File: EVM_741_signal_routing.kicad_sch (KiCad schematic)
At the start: 51 parts, among them J1 offset+, J10 out_a, J11 out_j, J12 out_j, J13 Vcc+_a, J14 Vcc-_a, J2 in-, J3 in+, J4 Vcc-, J5 offset-, J6 out, J7 Vcc+, J8 in+_a, J9 in-_a, Q1 MMBT3904, Q10 MMBT3904, Q11 MMBT3904, Q12 MMBT3906, Q13 MMBT3906, Q14 MMBT3904, Q15 MMBT3904, Q16 MMBT3904, Q17 MMBT3904, Q18 MMBT3904, Q2 MMBT3904, Q20 MMBT3906, Q22 MMBT3904, Q3 MMBT3906, Q4 MMBT3906, Q5 MMBT3904, Q6 MMBT3904, Q7 MMBT3904, Q8 MMBT3906, Q9 MMBT3906

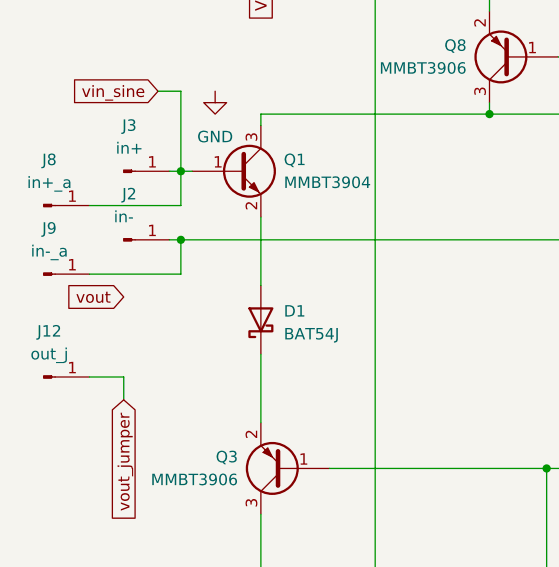
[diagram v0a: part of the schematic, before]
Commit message: added spice sim lib
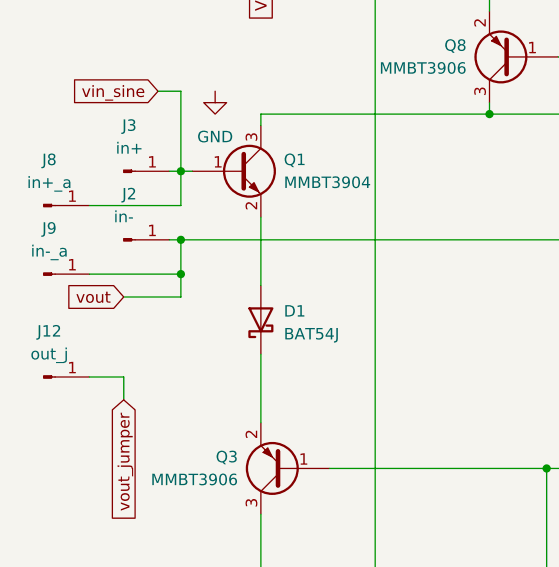
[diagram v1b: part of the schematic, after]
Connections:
- net vout: now also J2.1 (Pin_1), J9.1 (Pin_1), Q2.1 (B)
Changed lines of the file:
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@@
   (junction (at 182.88 58.42) (diameter 0) (color 0 0 0 0)
   )
+  (junction (at 34.29 57.15) (diameter 0) (color 0 0 0 0)
+  )
   (junction (at 55.88 21.59) (diameter 0) (color 0 0 0 0)
   )
@@
     (stroke (width 0) (type default))
   )
+  (wire (pts (xy 27.94 59.69) (xy 34.29 59.69))
+    (stroke (width 0) (type default))
+  )
   (wire (pts (xy 127 109.22) (xy 132.08 109.22))
     (stroke (width 0) (type default))
@@
   )
   (wire (pts (xy 233.68 63.5) (xy 233.68 78.74))
+    (stroke (width 0) (type default))
+  )
+  (wire (pts (xy 34.29 59.69) (xy 34.29 57.15))
     (stroke (width 0) (type default))
   )
@@
       (effects (font (size 1.27 1.27)) hide)
     )
-    (property "Sim.Library" "D:\\hw_things\\EVM_741_spice.lib" (at 43.18 62.23 0)
+    (property "Sim.Library" "${KIPRJMOD}\\EVM_741_spice.lib" (at 43.18 62.23 0)
       (effects (font (size 1.27 1.27)) hide)
     )
@@
       (effects (font (size 1.27 1.27)) (justify left) hide)
     )
-    (property "Sim.Library" "D:\\hw_things\\EVM_741_spice.lib" (at 205.74 58.42 0)
+    (property "Sim.Library" "${KIPRJMOD}\\EVM_741_spice.lib" (at 205.74 58.42 0)
       (effects (font (size 1.27 1.27)) hide)
     )
@@
       (effects (font (size 1.27 1.27)) (justify left) hide)
     )
-    (property "Sim.Library" "D:\\hw_things\\EVM_741_spice.lib" (at 180.34 91.44 0)
+    (property "Sim.Library" "${KIPRJMOD}\\EVM_741_spice.lib" (at 180.34 91.44 0)
       (effects (font (size 1.27 1.27)) hide)
     )
@@
       (effects (font (size 1.27 1.27)) hide)
     )
-    (property "Sim.Library" "D:\\hw_things\\EVM_741_spice.lib" (at 93.98 62.23 0)
+    (property "Sim.Library" "${KIPRJMOD}\\EVM_741_spice.lib" (at 93.98 62.23 0)
       (effects (font (size 1.27 1.27)) hide)
     )
@@
       (effects (font (size 1.27 1.27)) (justify left) hide)
     )
-    (property "Sim.Library" "D:\\hw_things\\EVM_741_spice.lib" (at 205.74 99.06 0)
+    (property "Sim.Library" "${KIPRJMOD}\\EVM_741_spice.lib" (at 205.74 99.06 0)
       (effects (font (size 1.27 1.27)) hide)
     )
@@
       (effects (font (size 1.27 1.27)) (justify left) hide)
     )
-    (property "Sim.Library" "D:\\hw_things\\EVM_741_spice.lib" (at 251.46 104.14 0)
+    (property "Sim.Library" "${KIPRJMOD}\\EVM_741_spice.lib" (at 251.46 104.14 0)
       (effects (font (size 1.27 1.27)) hide)
     )
@@
       (effects (font (size 1.27 1.27)) (justify left) hide)
     )
-    (property "Sim.Library" "D:\\hw_things\\EVM_741_spice.lib" (at 40.64 45.72 0)
+    (property "Sim.Library" "${KIPRJMOD}\\EVM_741_spice.lib" (at 40.64 45.72 0)
       (effects (font (size 1.27 1.27)) hide)
     )
@@
       (effects (font (size 1.27 1.27)) (justify left) hide)
     )
-    (property "Sim.Library" "D:\\hw_things\\EVM_741_spice.lib" (at 116.84 33.02 0)
+    (property "Sim.Library" "${KIPRJMOD}\\EVM_741_spice.lib" (at 116.84 33.02 0)
       (effects (font (size 1.27 1.27)) hide)
     )
@@
       (effects (font (size 1.27 1.27)) (justify left) hide)
     )
-    (property "Sim.Library" "D:\\hw_things\\EVM_741_spice.lib" (at 45.72 109.22 0)
+    (property "Sim.Library" "${KIPRJMOD}\\EVM_741_spice.lib" (at 45.72 109.22 0)
       (effects (font (size 1.27 1.27)) hide)
     )
@@
       (effects (font (size 1.27 1.27)) (justify left) hide)
     )
-    (property "Sim.Library" "D:\\hw_things\\EVM_741_spice.lib" (at 91.44 109.22 0)
+    (property "Sim.Library" "${KIPRJMOD}\\EVM_741_spice.lib" (at 91.44 109.22 0)
       (effects (font (size 1.27 1.27)) hide)
     )
@@
       (effects (font (size 1.27 1.27)) (justify left) hide)
     )
-    (property "Sim.Library" "D:\\hw_things\\EVM_741_spice.lib" (at 71.12 33.02 0)
+    (property "Sim.Library" "${KIPRJMOD}\\EVM_741_spice.lib" (at 71.12 33.02 0)
       (effects (font (size 1.27 1.27)) hide)
     )
@@
       (effects (font (size 1.27 1.27)) (justify left) hide)
     )
-    (property "Sim.Library" "D:\\hw_things\\EVM_741_spice.lib" (at 236.22 58.42 0)
+    (property "Sim.Library" "${KIPRJMOD}\\EVM_741_spice.lib" (at 236.22 58.42 0)
       (effects (font (size 1.27 1.27)) hide)
     )
@@
       (effects (font (size 1.27 1.27)) (justify left) hide)
     )
-    (property "Sim.Library" "D:\\hw_things\\EVM_741_spice.lib" (at 53.34 96.52 0)
+    (property "Sim.Library" "${KIPRJMOD}\\EVM_741_spice.lib" (at 53.34 96.52 0)
       (effects (font (size 1.27 1.27)) hide)
     )
@@
       (effects (font (size 1.27 1.27)) (justify left) hide)
     )
-    (property "Sim.Library" "D:\\hw_things\\EVM_741_spice.lib" (at 121.92 109.22 0)
+    (property "Sim.Library" "${KIPRJMOD}\\EVM_741_spice.lib" (at 121.92 109.22 0)
       (effects (font (size 1.27 1.27)) hide)
     )
@@
       (effects (font (size 1.27 1.27)) (justify left) hide)
     )
-    (property "Sim.Library" "D:\\hw_things\\EVM_741_spice.lib" (at 205.74 33.02 0)
+    (property "Sim.Library" "${KIPRJMOD}\\EVM_741_spice.lib" (at 205.74 33.02 0)
       (effects (font (size 1.27 1.27)) hide)
     )
@@
       (effects (font (size 1.27 1.27)) (justify left) hide)
     )
-    (property "Sim.Library" "D:\\hw_things\\EVM_741_spice.lib" (at 251.46 40.64 0)
+    (property "Sim.Library" "${KIPRJMOD}\\EVM_741_spice.lib" (at 251.46 40.64 0)
       (effects (font (size 1.27 1.27)) hide)
     )
@@
       (effects (font (size 1.27 1.27)) (justify left) hide)
     )
-    (property "Sim.Library" "D:\\hw_things\\EVM_741_spice.lib" (at 91.44 78.74 0)
+    (property "Sim.Library" "${KIPRJMOD}\\EVM_741_spice.lib" (at 91.44 78.74 0)
       (effects (font (size 1.27 1.27)) hide)
     )
@@
       (effects (font (size 1.27 1.27)) (justify left) hide)
     )
-    (property "Sim.Library" "D:\\hw_things\\EVM_741_spice.lib" (at 142.24 109.22 0)
+    (property "Sim.Library" "${KIPRJMOD}\\EVM_741_spice.lib" (at 142.24 109.22 0)
       (effects (font (size 1.27 1.27)) hide)
     )
@@
       (effects (font (size 1.27 1.27)) (justify left) hide)
     )
-    (property "Sim.Library" "D:\\hw_things\\EVM_741_spice.lib" (at 147.32 33.02 0)
+    (property "Sim.Library" "${KIPRJMOD}\\EVM_741_spice.lib" (at 147.32 33.02 0)
       (effects (font (size 1.27 1.27)) hide)
     )
@@
       (effects (font (size 1.27 1.27)) (justify left) hide)
     )
-    (property "Sim.Library" "D:\\hw_things\\EVM_741_spice.lib" (at 45.72 78.74 0)
+    (property "Sim.Library" "${KIPRJMOD}\\EVM_741_spice.lib" (at 45.72 78.74 0)
       (effects (font (size 1.27 1.27)) hide)
     )
@@
       (effects (font (size 1.27 1.27)) (justify left) hide)
     )
-    (property "Sim.Library" "D:\\hw_things\\EVM_741_spice.lib" (at 172.72 116.84 0)
+    (property "Sim.Library" "${KIPRJMOD}\\EVM_741_spice.lib" (at 172.72 116.84 0)
       (effects (font (size 1.27 1.27)) hide)
     )
@@
       (effects (font (size 1.27 1.27)) (justify left) hide)
     )
-    (property "Sim.Library" "D:\\hw_things\\EVM_741_spice.lib" (at 96.52 45.72 0)
-      (effects (font (size 1.27 1.27)) hide)
-    )
+    (property "Sim.Library" "${KIPRJMOD}\\EVM_741_spice.lib" (at 96.52 45.72 0)
+      (effects (font (size 1.27 1.27)) hide)
+    )

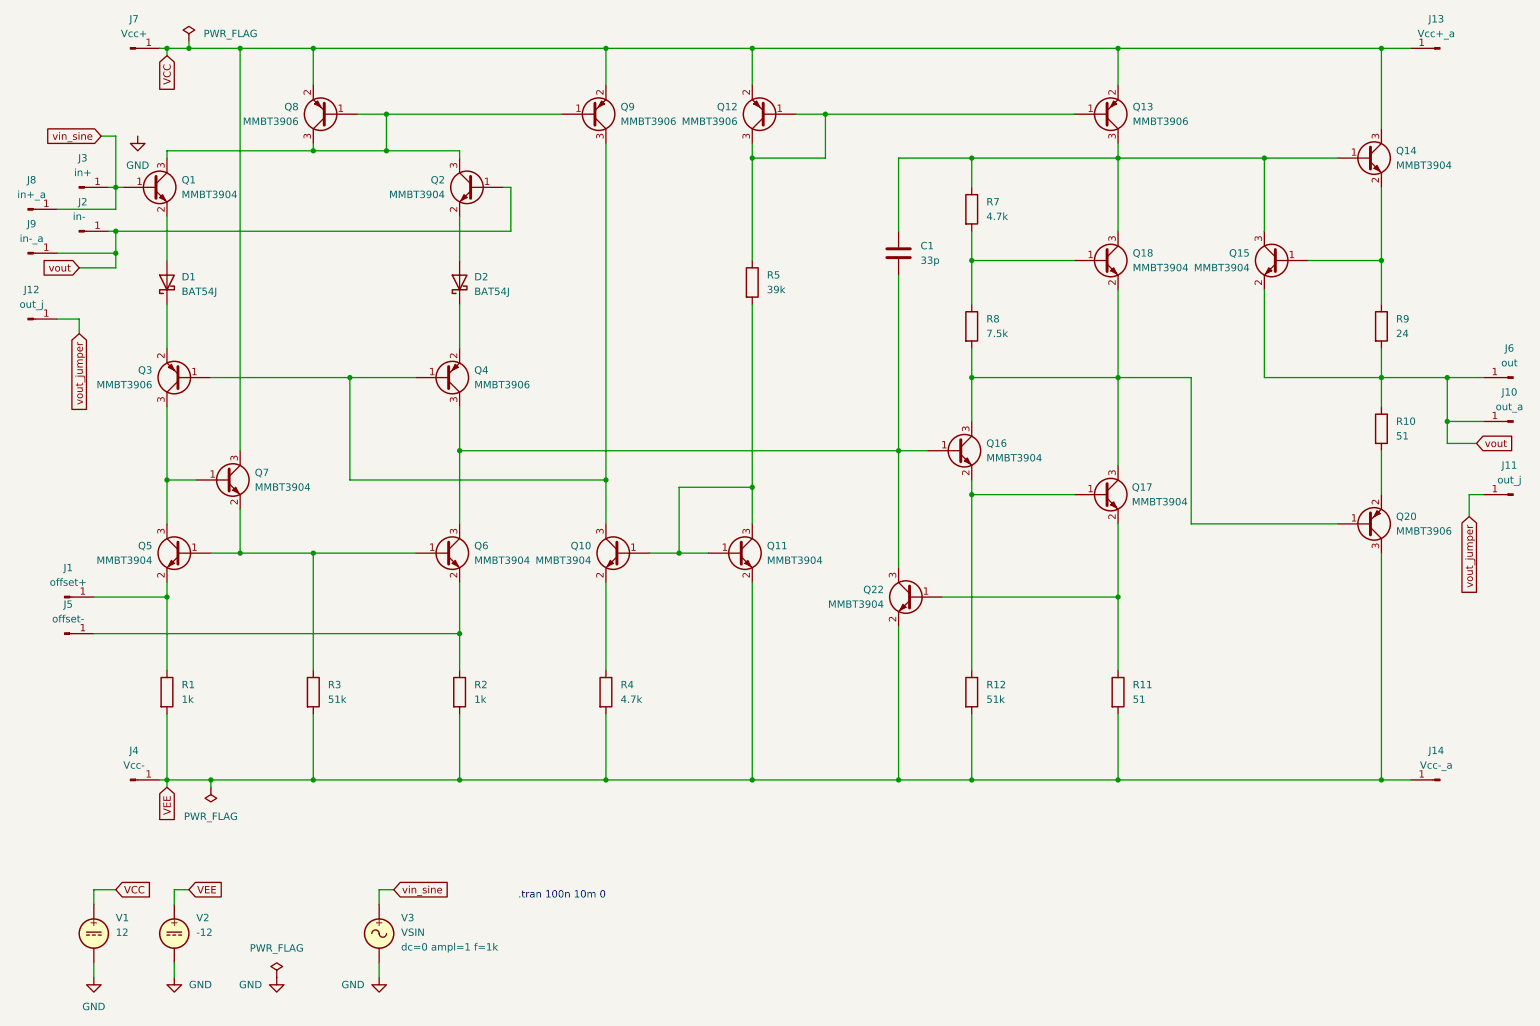
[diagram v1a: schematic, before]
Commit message: fixed silkscreen
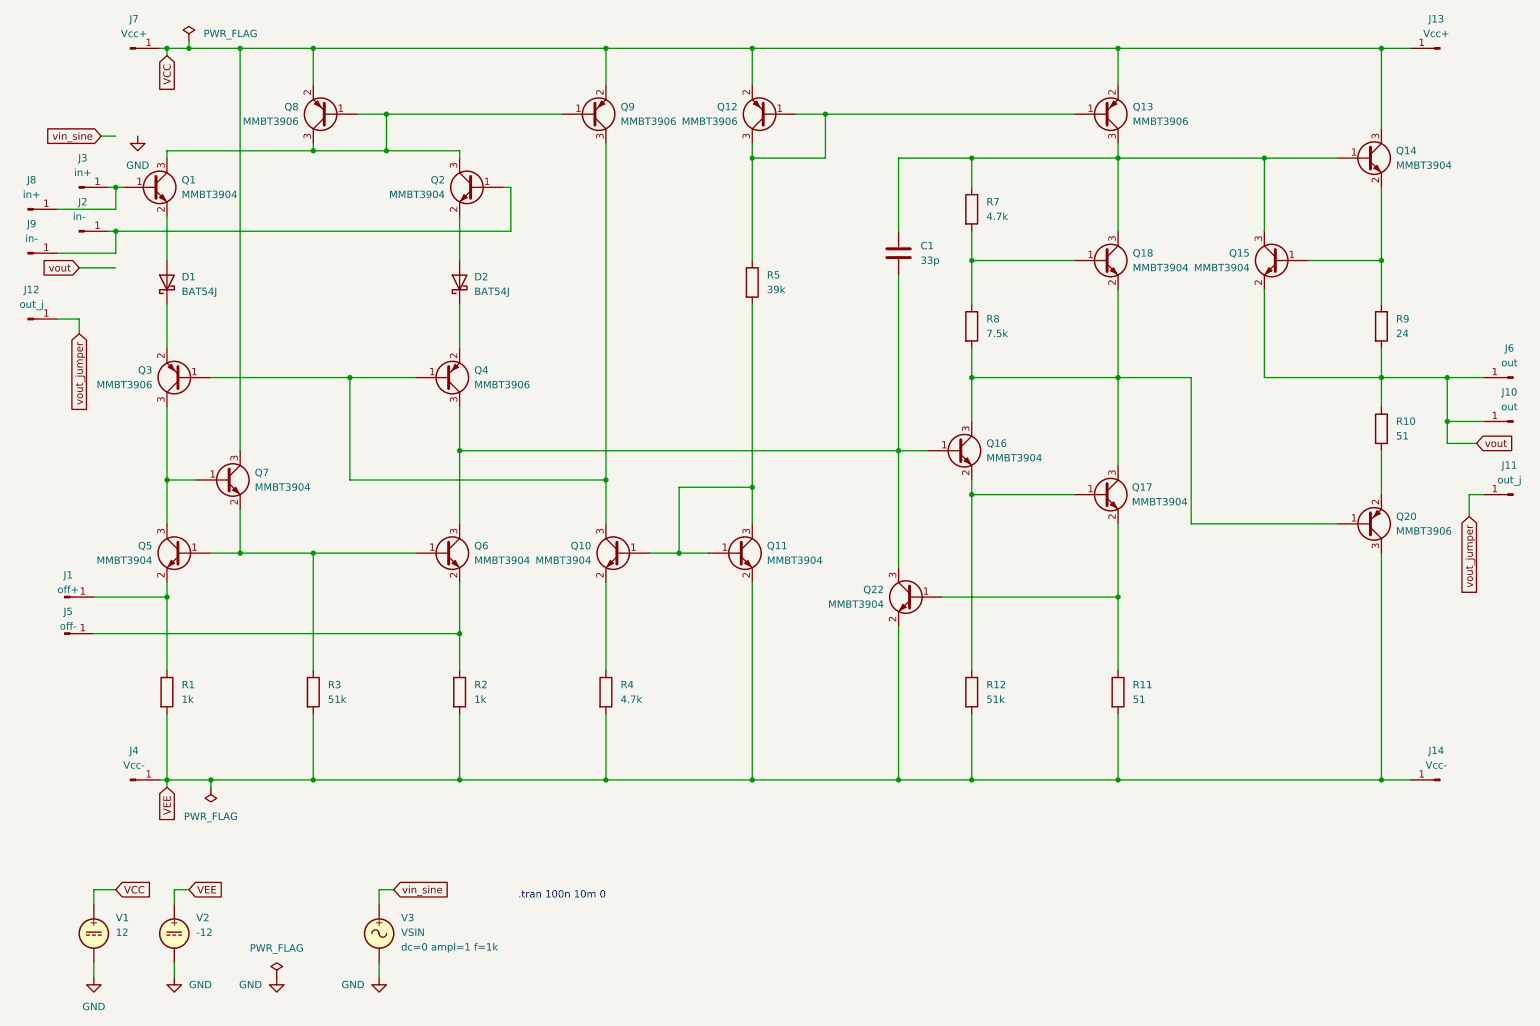
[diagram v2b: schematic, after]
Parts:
- J1: value offset+ -> off+
- J10: value out_a -> out
- J13: value Vcc+_a -> Vcc+
- J14: value Vcc-_a -> Vcc-
- J5: value offset- -> off-
- J8: value in+_a -> in+
- J9: value in-_a -> in-
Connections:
- net vin_sine: no longer J3.1 (Pin_1), J8.1 (Pin_1), Q1.1 (B)
- net vout: no longer J2.1 (Pin_1), J9.1 (Pin_1), Q2.1 (B)
- new net: J3.1 (Pin_1), J8.1 (Pin_1), Q1.1 (B)
- new net: J2.1 (Pin_1), J9.1 (Pin_1), Q2.1 (B)
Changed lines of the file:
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@@
   (junction (at 182.88 58.42) (diameter 0) (color 0 0 0 0)
   )
-  (junction (at 34.29 57.15) (diameter 0) (color 0 0 0 0)
-  )
   (junction (at 55.88 21.59) (diameter 0) (color 0 0 0 0)
   )
@@
     (stroke (width 0) (type default))
   )
-  (wire (pts (xy 34.29 59.69) (xy 34.29 57.15))
-    (stroke (width 0) (type default))
-  )
   (wire (pts (xy 27.94 68.58) (xy 24.13 68.58))
     (stroke (width 0) (type default))
@@
   )
   (wire (pts (xy 170.18 53.34) (xy 170.18 40.64))
-    (stroke (width 0) (type default))
-  )
-  (wire (pts (xy 34.29 36.83) (xy 34.29 45.72))
     (stroke (width 0) (type default))
   )
@@
       (effects (font (size 1.27 1.27)))
     )
-    (property "Value" "Vcc-_a" (at 263.525 146.05 0)
+    (property "Value" "Vcc-" (at 263.525 146.05 0)
       (effects (font (size 1.27 1.27)))
     )
@@
       (effects (font (size 1.27 1.27)))
     )
-    (property "Value" "in+_a" (at 19.685 46.99 0)
+    (property "Value" "in+" (at 19.685 46.99 0)
       (effects (font (size 1.27 1.27)))
     )
@@
   (symbol (lib_id "Connector:Conn_01x01_Male") (at 25.4 116.84 0) (unit 1)
     (in_bom yes) (on_board yes) (dnp no) (fields_autoplaced)
-    (property "Reference" "J1" (at 26.035 111.76 0)
-      (effects (font (size 1.27 1.27)))
-    )
-    (property "Value" "offset+" (at 26.035 114.3 0)
+    (property "Reference" "J1" (at 26.035 113.03 0)
+      (effects (font (size 1.27 1.27)))
+    )
+    (property "Value" "off+" (at 26.035 115.57 0)
       (effects (font (size 1.27 1.27)))
     )
@@
       (effects (font (size 1.27 1.27)))
     )
-    (property "Value" "Vcc+_a" (at 263.525 19.05 0)
+    (property "Value" "Vcc+" (at 263.525 19.05 0)
       (effects (font (size 1.27 1.27)))
     )
@@
       (effects (font (size 1.27 1.27)))
     )
-    (property "Value" "in-_a" (at 19.685 54.61 0)
+    (property "Value" "in-" (at 19.685 54.61 0)
       (effects (font (size 1.27 1.27)))
     )
@@
       (effects (font (size 1.27 1.27)))
     )
-    (property "Value" "out_a" (at 276.225 83.82 0)
+    (property "Value" "out" (at 276.225 83.82 0)
       (effects (font (size 1.27 1.27)))
     )
@@
   (symbol (lib_id "Connector:Conn_01x01_Male") (at 25.4 123.19 0) (unit 1)
     (in_bom yes) (on_board yes) (dnp no) (fields_autoplaced)
-    (property "Reference" "J5" (at 26.035 118.11 0)
-      (effects (font (size 1.27 1.27)))
-    )
-    (property "Value" "offset-" (at 26.035 120.65 0)
-      (effects (font (size 1.27 1.27)))
-    )
+    (property "Reference" "J5" (at 26.035 119.38 0)
+      (effects (font (size 1.27 1.27)))
+    )
+    (property "Value" "off-" (at 26.035 121.92 0)
+      (effects (font (size 1.27 1.27)))
+    )
